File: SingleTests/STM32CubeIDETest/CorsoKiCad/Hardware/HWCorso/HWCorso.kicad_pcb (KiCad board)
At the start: 4 copper layers, 147.6 x 102 mm, 47 parts, among them J1 USB_B_Mini, J2 BATTERY, J3 I2C_CONN, J4 SWD_CONN, J5 USART6_CONN, Q1 AO3401A, SW1 SW_SPDT, U1 STM32F401RCT6, U2 MP2359DJ-LF-Z, U3 USBLC6-2SC6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

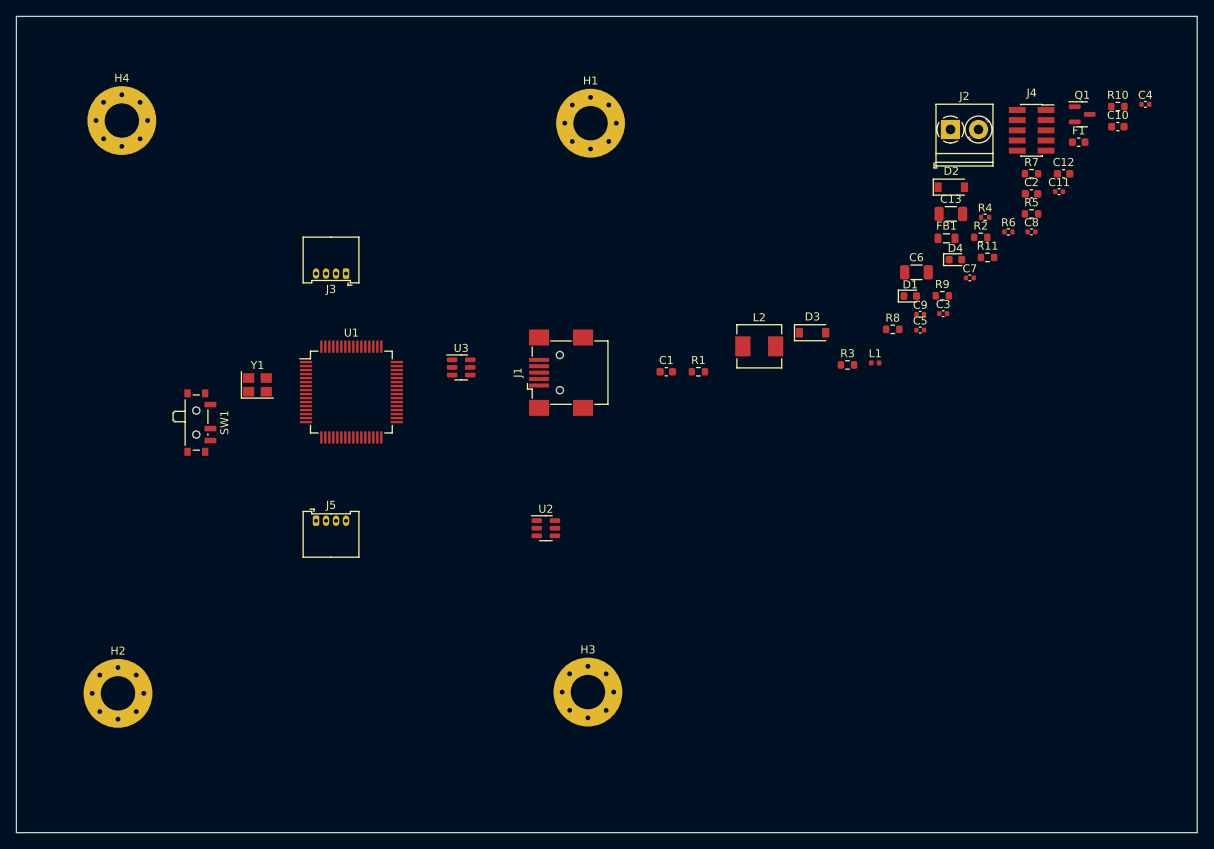
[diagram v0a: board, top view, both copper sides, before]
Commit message: Posizionamento dei componenti
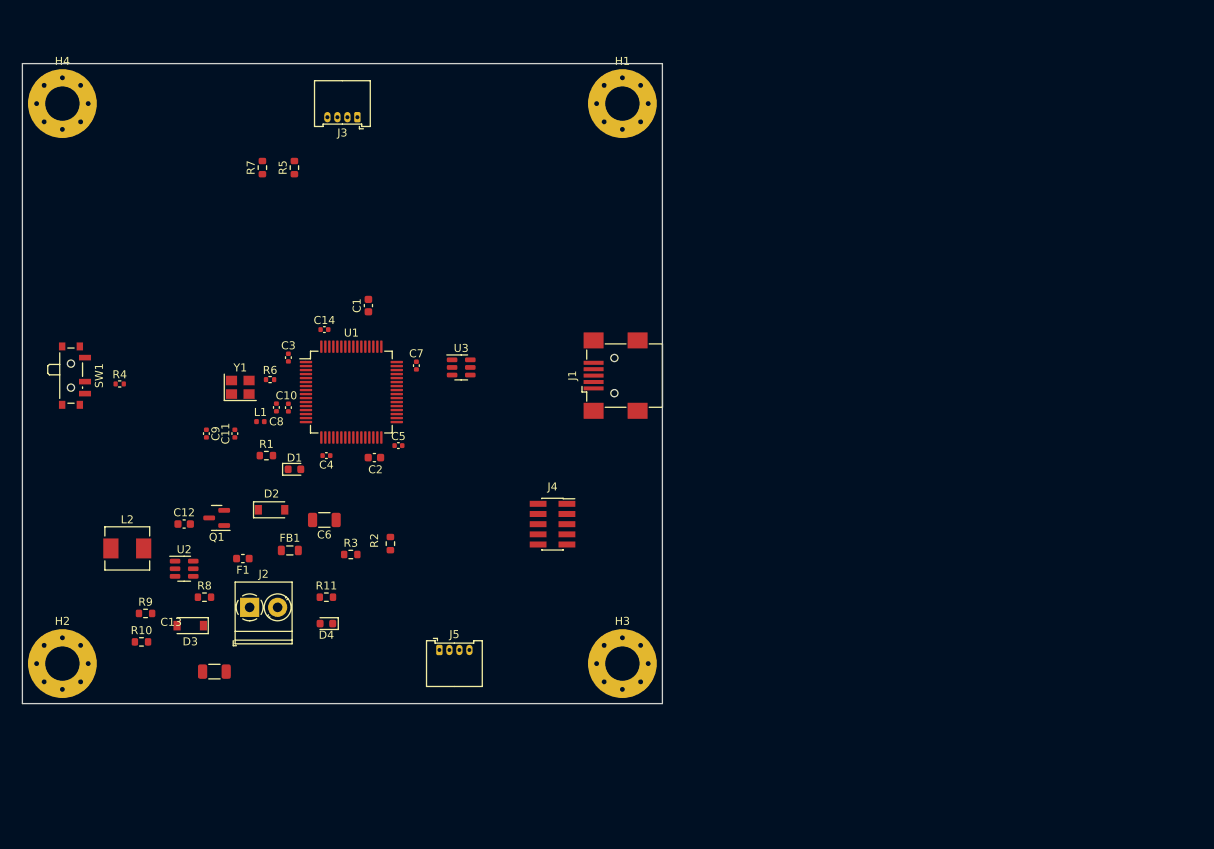
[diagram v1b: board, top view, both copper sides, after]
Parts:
- added C14: 100n, Capacitor_SMD:C_0402_1005Metric, F.Cu at (67.8, 91.2)
- C10: footprint Capacitor_SMD:C_0603_1608Metric -> Capacitor_SMD:C_0402_1005Metric
- moved R10 139.2 mm to (44.9, 130.3)
- moved Q1 119.4 mm to (54.3, 114.8), turned to 180 degrees
- moved C12 118.3 mm to (50.2, 115.6)
- moved F1 116.7 mm to (57.6, 119.9), turned to 180 degrees
- moved C4 111.4 mm to (68.0, 107.0), turned to 180 degrees
- moved R4 110.2 mm to (42.2, 98.0)
- moved C10 109.5 mm to (63.2, 101.0), turned to 90 degrees
- moved C13 108.4 mm to (54.0, 134.0)
- moved C11 107.4 mm to (56.6, 104.2), turned to 90 degrees
- moved R9 107.2 mm to (45.4, 126.7)
- moved J2 106.0 mm to (58.4, 126.0)
- moved C8 96.9 mm to (61.8, 101.0), turned to 90 degrees
- moved R7 96.1 mm to (60.0, 71.0), turned to 90 degrees
- moved R6 94.1 mm to (61.0, 97.5)
- moved D2 94.1 mm to (61.1, 113.8)
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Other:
- board size 147.6 x 102 mm -> 80 x 80 mm

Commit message: Layout della scheda
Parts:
- moved R10 46.8 mm to (89.5, 116.0), turned to -90 degrees
- moved R9 43.7 mm to (87.8, 116.0), turned to 90 degrees
- moved J2 43.3 mm to (95.3, 103.2), turned to 90 degrees
- moved D3 40.6 mm to (81.5, 101.5), turned to 0 degrees
- moved J4 39.8 mm to (83.2, 78.0), turned to 90 degrees
- moved U2 38.0 mm to (86.8, 110.8), turned to 90 degrees
- moved L2 37.1 mm to (79.5, 111.5), turned to -90 degrees
- moved Q1 36.7 mm to (88.8, 102.2), turned to -90 degrees
- moved D4 35.9 mm to (82.2, 95.0)
- moved F1 35.7 mm to (86.0, 98.2)
- moved R8 34.1 mm to (85.8, 116.0), turned to -90 degrees
- moved C12 33.6 mm to (83.5, 111.0), turned to 90 degrees
- moved D2 31.0 mm to (86.5, 96.0), turned to 180 degrees
- moved R11 30.9 mm to (82.2, 97.2)
- moved C13 30.6 mm to (79.2, 116.8), turned to 180 degrees
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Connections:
- F1 pad 1: +12V -> Net-(D2-Pad1)
- F1 pad 2: Net-(Q1-Pad3) -> Net-(F1-Pad2)
- FB1 pad 1: Net-(D2-Pad1) -> Net-(F1-Pad2)
- Q1 pad 3: Net-(Q1-Pad3) -> +12V
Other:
- board size 80 x 80 mm -> 46.8 x 46 mm

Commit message: Routing della scheda
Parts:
- J4: footprint Connector_PinSocket_1.27mm:PinSocket_2x05_P1.27mm_Vertical_SMD -> Connector_PinHeader_1.27mm:PinHeader_2x05_P1.27mm_Vertical_SMD
- moved C11 6.00 mm to (59.2, 101.2)
- moved C9 5.75 mm to (59.3, 95.0)
- moved D4 4.50 mm to (82.4, 99.5)
- moved R11 4.50 mm to (82.4, 101.8)
- moved D3 2.75 mm to (81.5, 104.2)
- moved R2 2.51 mm to (89.8, 108.8)
- moved R8 1.03 mm to (86.0, 115.0)
- moved R10 1.00 mm to (89.5, 115.0)
- moved R5 1.00 mm to (73.2, 86.2)
- moved R9 1.00 mm to (87.8, 115.0)
- moved C6 0.90 mm to (87.0, 105.8)
- moved R3 0.79 mm to (91.5, 108.8)
- moved R6 0.56 mm to (63.0, 98.0)
- moved R7 0.50 mm to (69.8, 86.2)
- moved SW1 0.50 mm to (57.0, 89.0)
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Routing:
- net GND: track 0.00 -> 69.2 mm, vias 0 -> 39
- net BUCK_VOUT_3V3: track 0.05 -> 44.8 mm, vias 0 -> 23
- net NRST: track 0.00 -> 33.9 mm, vias 0 -> 4
- net SWO: track 0.00 -> 24.2 mm
- net SWDIO: track 0.00 -> 22.2 mm
- net unconnected-(J1-Pad6): track 0.00 -> 19.8 mm
- net USART6_TX: track 0.00 -> 19.3 mm, vias 0 -> 2
- net USART6_RX: track 0.00 -> 18.0 mm, vias 0 -> 2
- net SWCLK: track 0.00 -> 17.4 mm
- net I2C1_SCL: track 0.00 -> 15.3 mm
- net I2C1_SDA: track 0.00 -> 14.5 mm
- net +5V: track 0.00 -> 13.8 mm
- net USB_D+: track 0.00 -> 12.6 mm
- net BUCK_SW: track 0.00 -> 12.2 mm
- net USB_D-: track 0.00 -> 11.8 mm
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- added copper zone on In2.Cu, net BUCK_VOUT_3V3
- added copper zone on In1.Cu, net GND
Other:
- board size 46.8 x 46 mm -> 48.2 x 47.5 mm
- board text added: "+"
- board text added: "BOOT"
- board text added: "I2C"
- board text added: "POWER"
- board text added: "REV 1.0"
- board text added: "RUN"
- board text added: "RX"
- board text added: "SCL"
- board text added: "SDA"
- board text added: "STATUS"
- board text added: "SWD"
- board text added: "TX"
- board text added: "USART6"
- board text added: "USB"
- board text added: "https://github.com/GiovanniRaseraF"

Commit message: File BOM e traduzione del file XML in csv
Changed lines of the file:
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@@
       (outputformat 1)
       (mirror false)
-      (drillshape 1)
+      (drillshape 0)
       (scaleselection 1)
-      (outputdirectory "")
+      (outputdirectory "gerber/")
     )
   )
@@
     (fp_line (start 1.6 0.8) (end -1.6 0.8) (layer "F.Fab") (width 0.1))
     (fp_line (start -1.6 0.8) (end -1.6 -0.8) (layer "F.Fab") (width 0.1))
-    (pad "1" smd roundrect (at -1.475 0 180) (size 1.15 1.8) (layers "F.Cu" "F.Paste" "F.Mask") (roundrect_rratio 0.217391)
+    (pad "1" smd roundrect (at -1.475 0 180) (size 1.15 1.8) (layers "F.Cu" "F.Paste" "F.Mask") (roundrect_rratio 0.2173913043)
       (net 2 "GND") (pintype "passive"))
-    (pad "2" smd roundrect (at 1.475 0 180) (size 1.15 1.8) (layers "F.Cu" "F.Paste" "F.Mask") (roundrect_rratio 0.217391)
+    (pad "2" smd roundrect (at 1.475 0 180) (size 1.15 1.8) (layers "F.Cu" "F.Paste" "F.Mask") (roundrect_rratio 0.2173913043)
       (net 1 "BUCK_VOUT_3V3") (pintype "passive"))
     (model "${KICAD6_3DMODEL_DIR}/Capacitor_SMD.3dshapes/C_1206_3216Metric.wrl"
@@
     (fp_line (start 1.6 0.8) (end -1.6 0.8) (layer "F.Fab") (width 0.1))
     (fp_line (start -1.6 0.8) (end -1.6 -0.8) (layer "F.Fab") (width 0.1))
-    (pad "1" smd roundrect (at -1.475 0) (size 1.15 1.8) (layers "F.Cu" "F.Paste" "F.Mask") (roundrect_rratio 0.217391)
+    (pad "1" smd roundrect (at -1.475 0) (size 1.15 1.8) (layers "F.Cu" "F.Paste" "F.Mask") (roundrect_rratio 0.2173913043)
       (net 4 "BUCK_IN") (pintype "passive"))
-    (pad "2" smd roundrect (at 1.475 0) (size 1.15 1.8) (layers "F.Cu" "F.Paste" "F.Mask") (roundrect_rratio 0.217391)
+    (pad "2" smd roundrect (at 1.475 0) (size 1.15 1.8) (layers "F.Cu" "F.Paste" "F.Mask") (roundrect_rratio 0.2173913043)
       (net 2 "GND") (pintype "passive"))
     (model "${KICAD6_3DMODEL_DIR}/Capacitor_SMD.3dshapes/C_1206_3216Metric.wrl"
